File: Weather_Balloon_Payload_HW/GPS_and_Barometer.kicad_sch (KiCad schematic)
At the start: 14 parts, among them J2 Conn_01x08, U5 MAX-M8C, U6 MS5607-02BA, U7 MCP9808_DFN

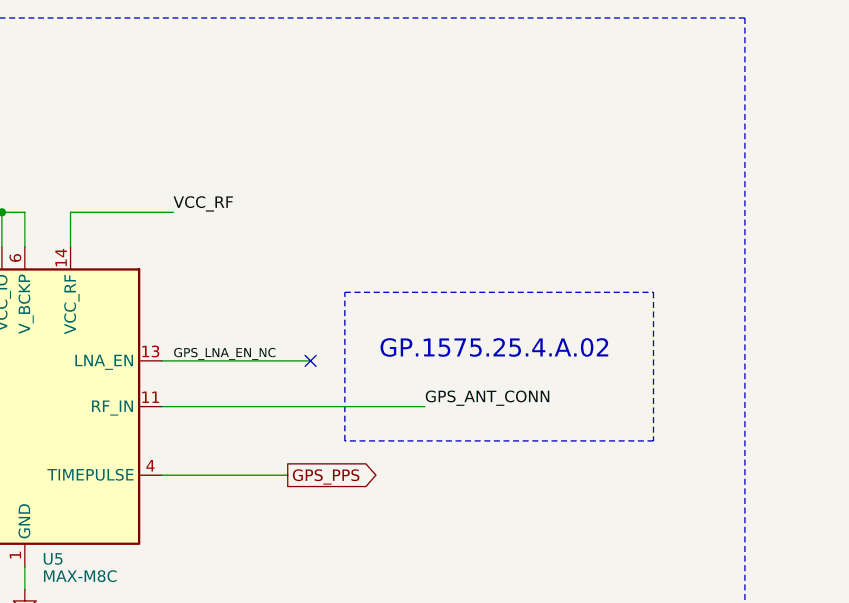
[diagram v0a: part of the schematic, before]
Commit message: Update README, block diagrams, schem. Begin layout
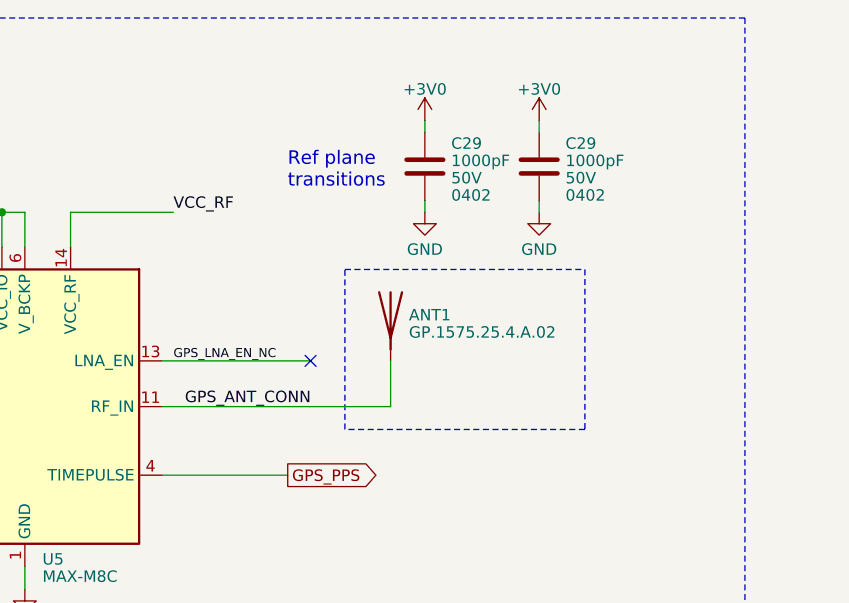
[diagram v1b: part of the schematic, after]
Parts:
- added ANT1: GP.1575.25.4.A.02, Repowered_Antennas:Taoglas_GP.1575.25.4.A.02, symbol Device:Antenna
- added C29 (x2): 1000pF, Capacitor_SMD:C_0402_1005Metric, symbol Device:C
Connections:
- net +3V0: now also C29.2, C29.2
- net GND: now also C29.1, C29.1
- net GPS_ANT_CONN: now also ANT1.1 (A)
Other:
- note added: "Ref plane transitions"
- note removed: "GP.1575.25.4.A.02"

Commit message: Add fabrication files
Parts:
- removed U7: MCP9808_DFN, Package_DFN_QFN:DFN-8-1EP_3x2mm_P0.5mm_EP1.7x1.4mm, symbol Sensor_Temperature:MCP9808_DFN
- added U18: MCP9808_MSOP, Package_SO:MSOP-8_3x3mm_P0.65mm, symbol Sensor_Temperature:MCP9808_MSOP
- R7: JLCPCB Part # (none) -> C153104; Manufacturer (none) -> TA-I Tech; Mfr. Part # (none) -> RM04JTN102
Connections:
- net +3V0: now also U18.8 (V_{DD})
- net GND: now also U18.4 (GND), U18.5 (A2), U18.6 (A1), U18.7 (A0)
- net I2C_SCL: now also U18.2 (SCL)
- net I2C_SDA: now also U18.1 (SDA)
- net TSNS_INT_ALERT: now also U18.3 (Alert)
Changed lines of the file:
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@@
   (junction (at 290.83 176.53) (diameter 0) (color 0 0 0 0)
-  )
-  (junction (at 304.8 186.69) (diameter 0) (color 0 0 0 0)
   )
   (junction (at 144.78 153.67) (diameter 0) (color 0 0 0 0)
@@
     (stroke (width 0) (type default))
   )
-  (wire (pts (xy 307.34 186.69) (xy 304.8 186.69))
-    (stroke (width 0) (type default))
-  )
   (wire (pts (xy 309.88 74.93) (xy 302.26 74.93))
     (stroke (width 0) (type default))
   )
-  (wire (pts (xy 304.8 184.15) (xy 304.8 186.69))
+  (wire (pts (xy 304.8 184.15) (xy 304.8 189.23))
     (stroke (width 0) (type default))
   )
@@
     (stroke (width 0) (type default))
   )
-  (wire (pts (xy 304.8 186.69) (xy 304.8 189.23))
-    (stroke (width 0) (type default))
-  )
   (wire (pts (xy 76.2 91.44) (xy 114.3 91.44))
     (stroke (width 0) (type default))
@@
   )
   (wire (pts (xy 134.62 59.69) (xy 146.05 59.69))
-    (stroke (width 0) (type default))
-  )
-  (wire (pts (xy 307.34 184.15) (xy 307.34 186.69))
     (stroke (width 0) (type default))
   )
@@
       (effects (font (size 1.27 1.27)) hide)
     )
-    (property "JLCPCB Part #" "~" (at 279.4 97.79 0)
-      (effects (font (size 1.27 1.27)) hide)
-    )
-    (property "Manufacturer" "~" (at 279.4 97.79 0)
-      (effects (font (size 1.27 1.27)) hide)
-    )
-    (property "Mfr. Part #" "~" (at 279.4 97.79 0)
+    (property "JLCPCB Part #" "C153104" (at 279.4 97.79 0)
+      (effects (font (size 1.27 1.27)) hide)
+    )
+    (property "Manufacturer" "TA-I Tech" (at 279.4 97.79 0)
+      (effects (font (size 1.27 1.27)) hide)
+    )
+    (property "Mfr. Part #" "RM04JTN102" (at 279.4 97.79 0)
       (effects (font (size 1.27 1.27)) hide)
     )
@@
       (effects (font (size 1.27 1.27)) hide)
     )
-    (property "JLCPCB Part #" "~" (at 279.4 92.71 0)
-      (effects (font (size 1.27 1.27)) hide)
-    )
-    (property "Manufacturer" "~" (at 279.4 92.71 0)
-      (effects (font (size 1.27 1.27)) hide)
-    )
-    (property "Mfr. Part #" "~" (at 279.4 92.71 0)
+    (property "JLCPCB Part #" "C153104" (at 279.4 92.71 0)
+      (effects (font (size 1.27 1.27)) hide)
+    )
+    (property "Manufacturer" "TA-I Tech" (at 279.4 92.71 0)
+      (effects (font (size 1.27 1.27)) hide)
+    )
+    (property "Mfr. Part #" "RM04JTN102" (at 279.4 92.71 0)
       (effects (font (size 1.27 1.27)) hide)
     )
@@
     )
   )
-  (symbol (lib_id "Sensor_Temperature:MCP9808_DFN") (at 304.8 171.45 0) (unit 1)
+  (symbol (lib_id "Sensor_Temperature:MCP9808_MSOP") (at 304.8 171.45 0) (unit 1)
     (in_bom yes) (on_board yes) (dnp no)
-    (property "Reference" "U7" (at 312.42 158.75 0)
-      (effects (font (size 1.27 1.27)))
-    )
-    (property "Value" "MCP9808_DFN" (at 316.23 184.15 0)
-      (effects (font (size 1.27 1.27)))
-    )
-    (property "Footprint" "Package_DFN_QFN:DFN-8-1EP_3x2mm_P0.5mm_EP1.7x1.4mm" (at 304.8 171.45 0)
-      (effects (font (size 1.27 1.27)) hide)
-    )
-    (property "Datasheet" "http://ww1.microchip.com/downloads/en/DeviceDoc/MCP9808-0.5C-Maximum-Accuracy-Digital-Temperature-Sensor-Data-Sheet-DS20005095B.pdf" (at 298.45 160.02 0)
+    (property "Reference" "U18" (at 311.15 158.75 0)
+      (effects (font (size 1.27 1.27)))
+    )
+    (property "Value" "MCP9808_MSOP" (at 320.04 182.88 0)
+      (effects (font (size 1.27 1.27)))
+    )
+    (property "Footprint" "Package_SO:MSOP-8_3x3mm_P0.65mm" (at 304.8 171.45 0)
+      (effects (font (size 1.27 1.27)) hide)
+    )
+    (property "Datasheet" "http://ww1.microchip.com/downloads/en/DeviceDoc/22203b.pdf" (at 298.45 160.02 0)
+      (effects (font (size 1.27 1.27)) hide)
+    )
+    (property "Description" "MSOP-8  Temperature Sensors ROHS" (at 304.8 171.45 0)
+      (effects (font (size 1.27 1.27)) hide)
+    )
+    (property "JLCPCB Part #" "C129490" (at 304.8 171.45 0)
+      (effects (font (size 1.27 1.27)) hide)
+    )
+    (property "Manufacturer" "Microchip Tech" (at 304.8 171.45 0)
+      (effects (font (size 1.27 1.27)) hide)
+    )
+    (property "Mfr. Part #" "MCP9808T-E/MS" (at 304.8 171.45 0)
       (effects (font (size 1.27 1.27)) hide)
     )
@@
     (pin "7")
     (pin "8")
-    (pin "9")
-    (instances
-      (project "Weather_Balloon_Payload_HW"
-        (path "/5c4ed951-5674-406c-8bab-ae3e3237b79b/aba2900f-3f29-480d-bd2f-eda335f8728f"
-          (reference "U7") (unit 1)
+    (instances
+      (project "Weather_Balloon_Payload_HW"
+        (path "/5c4ed951-5674-406c-8bab-ae3e3237b79b/aba2900f-3f29-480d-bd2f-eda335f8728f"
+          (reference "U18") (unit 1)
         )
       )
@@
       (effects (font (size 1.27 1.27)) hide)
     )
-    (property "JLCPCB Part #" "~" (at 279.4 87.63 0)
-      (effects (font (size 1.27 1.27)) hide)
-    )
-    (property "Manufacturer" "~" (at 279.4 87.63 0)
-      (effects (font (size 1.27 1.27)) hide)
-    )
-    (property "Mfr. Part #" "~" (at 279.4 87.63 0)
-      (effects (font (size 1.27 1.27)) hide)
-    )
+    (property "JLCPCB Part #" "C153104" (at 279.4 87.63 0)
+      (effects (font (size 1.27 1.27)) hide)
+    )
+    (property "Manufacturer" "TA-I Tech" (at 279.4 87.63 0)
+      (effects (font (size 1.27 1.27)) hide)
+    )
+    (property "Mfr. Part #" "RM04JTN102" (at 279.4 87.63 0)
+      (effects (font (size 1.27 1.27)) hide)
+    )

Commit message: Antenna imped match files, boilerplate STM code
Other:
- note added: "I2C ADDR: 0x42"
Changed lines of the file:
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@@
     (effects (font (size 2.5 2.5)) (justify left bottom))
+  )
+  (text "I2C ADDR: 0x42" (at 90.17 102.87 0)
+    (effects (font (size 1.5 1.5)) (justify left bottom))
   )
   (text "Ref plane\ntransitions" (at 158.75 57.15 0)
